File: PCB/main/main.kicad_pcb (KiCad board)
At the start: 2 copper layers, 4 parts, among them J1 Conn_01x33_Female, J2 Conn_01x33_Female, J3 Conn_01x33_Female, J4 Conn_01x33_Female

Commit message: Design PCB
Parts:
- added BT1: 18650, Footprint_EEE3088F:18650_Holder, F.Cu at (128.0, 139.8)
- added C1: 0.1uF, Capacitor_SMD:C_0402_1005Metric, F.Cu at (171.6, 112.8)
- added C10: 100nF, Capacitor_SMD:C_0402_1005Metric, F.Cu at (86.9, 85.4)
- added C11: 4.7nF, Capacitor_SMD:C_0402_1005Metric, F.Cu at (91.5, 85.4)
- added C2: 22uF, Capacitor_SMD:C_0603_1608Metric, F.Cu at (167.2, 98.6)
- added C3: 330pF, Capacitor_SMD:C_0402_1005Metric, F.Cu at (159.0, 98.0)
- added C4: 0.1uF, Capacitor_SMD:C_0402_1005Metric, F.Cu at (133.0, 156.8)
- added C5: 100uF, Capacitor_SMD:C_1206_3216Metric, F.Cu at (133.0, 161.4)
- added C6: 33pF, Capacitor_SMD:C_0402_1005Metric, F.Cu at (151.2, 88.6)
- added C7: 10nF, Capacitor_SMD:C_0402_1005Metric, F.Cu at (158.2, 93.6)
- added C8: 33pF, Capacitor_SMD:C_0402_1005Metric, F.Cu at (151.4, 80.2)
- added C9: 0.1uF, Capacitor_SMD:C_0402_1005Metric, F.Cu at (151.8, 103.8)
- added D1: BAT54S, Diode_SMD:D_SOT-23_ANK, F.Cu at (177.8, 141.4)
- added D2: DIODE, Footprint_EEE3088F:DO-214AC_L4.3-W2.7-LS5.3-RD, F.Cu at (171.2, 99.6)
- added D3: ZMM5V1-M, Footprint_EEE3088F:LL-34_L3.5-W1.5-RD, F.Cu at (180.7, 112.2)
- added D4: LED, LED_SMD:LED_0603_1608Metric, F.Cu at (171.0, 93.2)
- added D5: ZMM4V7-M, Footprint_EEE3088F:LL-34_L3.5-W1.5-RD, F.Cu at (170.5, 153.2)
- added D6: DIODE, Footprint_EEE3088F:DO-214AC_L4.3-W2.7-LS5.3-RD, F.Cu at (160.0, 156.6)
- added D7: BZT52C3V0, Diode_SMD:D_SOD-123, F.Cu at (106.0, 97.8)
- added D8: LED, LED_SMD:LED_0603_1608Metric, F.Cu at (93.2, 93.2)
- added D9: LED, LED_SMD:LED_0603_1608Metric, F.Cu at (93.3, 116.3)
- added J1: Conn_01x03_Female, Connector_PinHeader_1.00mm:PinHeader_1x03_P1.00mm_Vertical, F.Cu at (180.0, 132.6)
- added JP1: SolderJumper_2_Bridged, Jumper:SolderJumper-2_P1.3mm_Bridged2Bar_Pad1.0x1.5mm, F.Cu at (175.8, 112.2)
- added JP10: SolderJumper_2_Bridged, Jumper:SolderJumper-2_P1.3mm_Bridged2Bar_Pad1.0x1.5mm, F.Cu at (148.0, 109.4)
- added JP2: SolderJumper_2_Bridged, Jumper:SolderJumper-2_P1.3mm_Bridged2Bar_Pad1.0x1.5mm, F.Cu at (175.3, 103.4)
- added JP3: SolderJumper_2_Bridged, Jumper:SolderJumper-2_P1.3mm_Bridged2Bar_Pad1.0x1.5mm, F.Cu at (173.6, 141.6)
- added JP4: SolderJumper_2_Bridged, Jumper:SolderJumper-2_P1.3mm_Bridged2Bar_Pad1.0x1.5mm, F.Cu at (133.2, 152.8)
- added JP5: SolderJumper_2_Bridged, Jumper:SolderJumper-2_P1.3mm_Bridged2Bar_Pad1.0x1.5mm, F.Cu at (88.9, 104.9)
- added JP6: SolderJumper_2_Bridged, Jumper:SolderJumper-2_P1.3mm_Bridged2Bar_Pad1.0x1.5mm, F.Cu at (88.8, 96.6)
- added JP7: SolderJumper_2_Bridged, Jumper:SolderJumper-2_P1.3mm_Bridged2Bar_Pad1.0x1.5mm, F.Cu at (166.8, 81.0)
- added JP8: SolderJumper_2_Bridged, Jumper:SolderJumper-2_P1.3mm_Bridged2Bar_Pad1.0x1.5mm, F.Cu at (167.0, 85.4)
- added JP9: SolderJumper_2_Bridged, Jumper:SolderJumper-2_P1.3mm_Bridged2Bar_Pad1.0x1.5mm, F.Cu at (143.4, 109.5)
- added K1: ADW11, Relay_THT:Relay_SPST_Omron-G5Q-1A, F.Cu at (155.6, 152.8)
- added Q1: AO3401A, Package_TO_SOT_SMD:SOT-23, F.Cu at (180.6, 104.0)
- added Q2: 2N3904, Package_TO_SOT_SMD:SOT-23, F.Cu at (166.2, 157.6)
- added Q3: FDS6690A, Package_SO:SOIC-8_3.9x4.9mm_P1.27mm, F.Cu at (102.6, 109.1)
- added R1: 100, Resistor_SMD:R_0603_1608Metric, F.Cu at (179.8, 108.2)
- added R10: 1k, Resistor_SMD:R_0402_1005Metric, F.Cu at (182.1, 153.2)
- added R11: 100k, Resistor_SMD:R_0402_1005Metric, F.Cu at (175.0, 153.3)
- added R12: 330, Resistor_SMD:R_0402_1005Metric, F.Cu at (97.1, 97.8)
- added R13: 330, Resistor_SMD:R_0402_1005Metric, F.Cu at (100.5, 97.8)
- added R14: 10k, Resistor_SMD:R_0402_1005Metric, F.Cu at (93.2, 89.2)
- added R15: 330, Resistor_SMD:R_0402_1005Metric, F.Cu at (93.6, 105.6)
- added R16: 220, Resistor_SMD:R_0402_1005Metric, F.Cu at (93.6, 109.1)
- added R17: 10k, Resistor_SMD:R_0402_1005Metric, F.Cu at (93.6, 112.9)
- added R2: 2M, Resistor_SMD:R_0805_2012Metric, F.Cu at (163.0, 97.9)
- added R3: 806K, Resistor_SMD:R_0402_1005Metric, F.Cu at (159.0, 101.4)
- added R4: 2.7k, Resistor_SMD:R_0402_1005Metric, F.Cu at (167.3, 93.2)
- added R5: 4.7k, Resistor_SMD:R_0402_1005Metric, F.Cu at (163.6, 93.2)
- added R6: 82, Resistor_SMD:R_0603_1608Metric, F.Cu at (171.0, 89.0)
- added R7: 10k, Resistor_SMD:R_0402_1005Metric, F.Cu at (154.1, 109.6)
- added R8: 10k, Resistor_SMD:R_0402_1005Metric, F.Cu at (154.1, 113.0)
- added R9: 150, Resistor_SMD:R_0402_1005Metric, F.Cu at (178.6, 153.2)
- added RV1: 50K, Footprint_EEE3088F:VG039NCHXTB503, F.Cu at (159.0, 107.4)
- added TP1: TestPoint, TestPoint:TestPoint_Pad_D1.0mm, B.Cu at (169.4, 148.4)
- added TP2: TestPoint, TestPoint:TestPoint_Pad_D1.0mm, B.Cu at (154.0, 98.5)
- added TP3: TestPoint, TestPoint:TestPoint_Pad_D1.0mm, B.Cu at (165.5, 90.2)
- added TP4: TestPoint, TestPoint:TestPoint_Pad_D1.0mm, B.Cu at (147.5, 147.1)
- added TP5: TestPoint, TestPoint:TestPoint_Pad_D1.0mm, B.Cu at (99.2, 102.4)
- added TP6: TestPoint, TestPoint:TestPoint_Pad_D1.0mm, B.Cu at (157.4, 112.3)
- added U1: LP2951-33DR, Package_SO:SOIC-8_3.9x4.9mm_P1.27mm, F.Cu at (169.2, 107.6)
- added U2: AMS1117, Package_TO_SOT_SMD:SOT-223-3_TabPin2, F.Cu at (125.0, 155.2)
- added U3: CH340G, Package_SO:SOIC-16_3.9x9.9mm_P1.27mm, F.Cu at (158.2, 85.0)
- added U4: USB_Micro_B, Footprint_EEE3088F:C404969_Micro_USB, F.Cu at (184.2, 96.5)
- added U5: AT24C256C-SSHL-T, Footprint_EEE3088F:SOIC-8_L4.9-W3.9-P1.27-LS6.0-BL, F.Cu at (147.2, 100.6)
- added U6: LM358DR2G, Package_SO:SOIC-8_3.9x4.9mm_P1.27mm, F.Cu at (178.6, 158.8)
- added U7: VL6180XV0NR_1, Footprint_EEE3088F:LGA-12_L4.8-W2.8-P0.75-BL, F.Cu at (88.8, 90.6)
- added U8: MCP9700T-ETT, Package_TO_SOT_SMD:SOT-23, F.Cu at (88.7, 110.2)
- added X1: 12MHz Crystal, Footprint_EEE3088F:OSC-SMD_4P-L3.2-W2.5-BL, F.Cu at (151.4, 84.2)
- J3: renamed from J2; footprint Connector_PinSocket_2.54mm:PinSocket_1x33_P2.54mm_Vertical -> Connector_PinHeader_2.54mm:PinHeader_1x33_P2.54mm_Vertical
- J4: renamed from J3; footprint Connector_PinSocket_2.54mm:PinSocket_1x33_P2.54mm_Vertical -> Connector_PinHeader_2.54mm:PinHeader_1x33_P2.54mm_Vertical
- renumbered J1 to J2, J4 to J5
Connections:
- net +3V0 renamed /+3V0
- net +5V renamed /+5V
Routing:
- net VDD: track 0.00 -> 212.7 mm, vias 0 -> 3
- net /Power/Battery +: track 0.00 -> 131.3 mm, vias 0 -> 2
- net /PB8: track 0.00 -> 110.9 mm, vias 0 -> 6
- net /PB7: track 0.00 -> 98.6 mm, vias 0 -> 2
- net /PB4: track 0.00 -> 90.4 mm
- net /microcontroller_interfacing/+5V: track 0.00 -> 86.5 mm
- net GND: track 0.00 -> 77.1 mm, vias 0 -> 12
- net /PA4: track 0.00 -> 62.4 mm, vias 0 -> 1
- net /PA9: track 0.00 -> 61.3 mm, vias 0 -> 2
- net /PA10: track 0.00 -> 58.2 mm, vias 0 -> 2
- net /Power/+5V (REVERSE PROTECTED): track 0.00 -> 49.9 mm, vias 0 -> 2
- net /PB1: track 0.00 -> 43.9 mm
- net /PB0: track 0.00 -> 43.6 mm, vias 0 -> 2
- net /Sensing/Proximity_Sensor/VCC: track 0.00 -> 33.6 mm
- net Net-(C8-Pad1): track 0.00 -> 27.0 mm, vias 0 -> 2
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- added copper zone on B.Cu, net (none)
- added copper zone on F.Cu, net GND
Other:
- board outline added: 100 x 100 mm
- board text added: "Heather, Kelvin, Noah Group 5"

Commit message: Fix DRC errors
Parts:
- J1: footprint Connector_PinHeader_1.00mm:PinHeader_1x03_P1.00mm_Vertical -> Connector_PinHeader_1.27mm:PinHeader_1x03_P1.27mm_Vertical

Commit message: pcb revive
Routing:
- net /Power/Battery +: track 131.3 -> 150.6 mm
- net Net-(C8-Pad1): track 27.0 -> 29.1 mm
- net /Sensing/Proximity_Sensor/VCC: track 33.7 -> 31.7 mm
- net Net-(C3-Pad2): track 20.6 -> 22.6 mm
- net VDD: track 212.8 -> 214.5 mm
- net Net-(D5-Pad1): track 15.5 -> 13.9 mm
- net /microcontroller_interfacing/D-: track 19.8 -> 21.1 mm
- net /PB7: track 98.6 -> 99.3 mm
- net /PB4: track 90.4 -> 90.9 mm

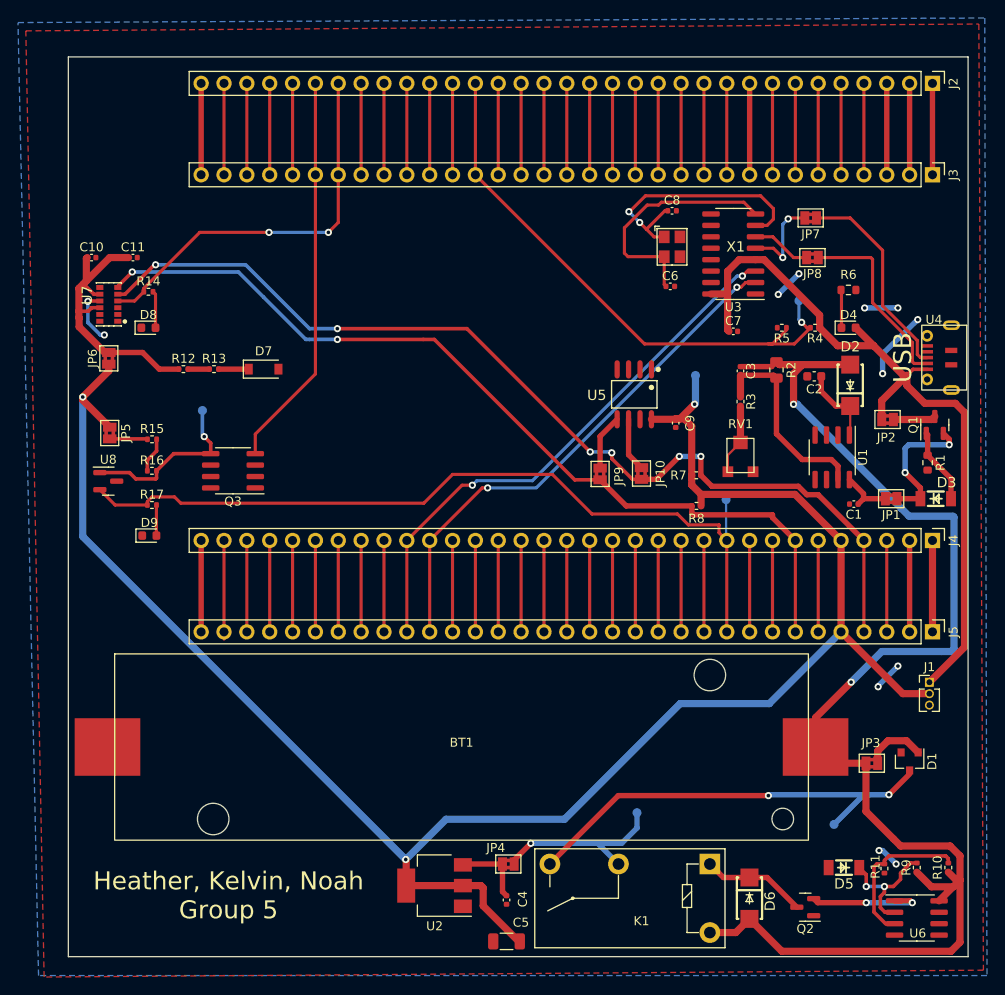
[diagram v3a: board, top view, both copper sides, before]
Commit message: Revert "pcb n"
This reverts commit 8727529f109f5bdd44d95993405a88df4b4ab9b1
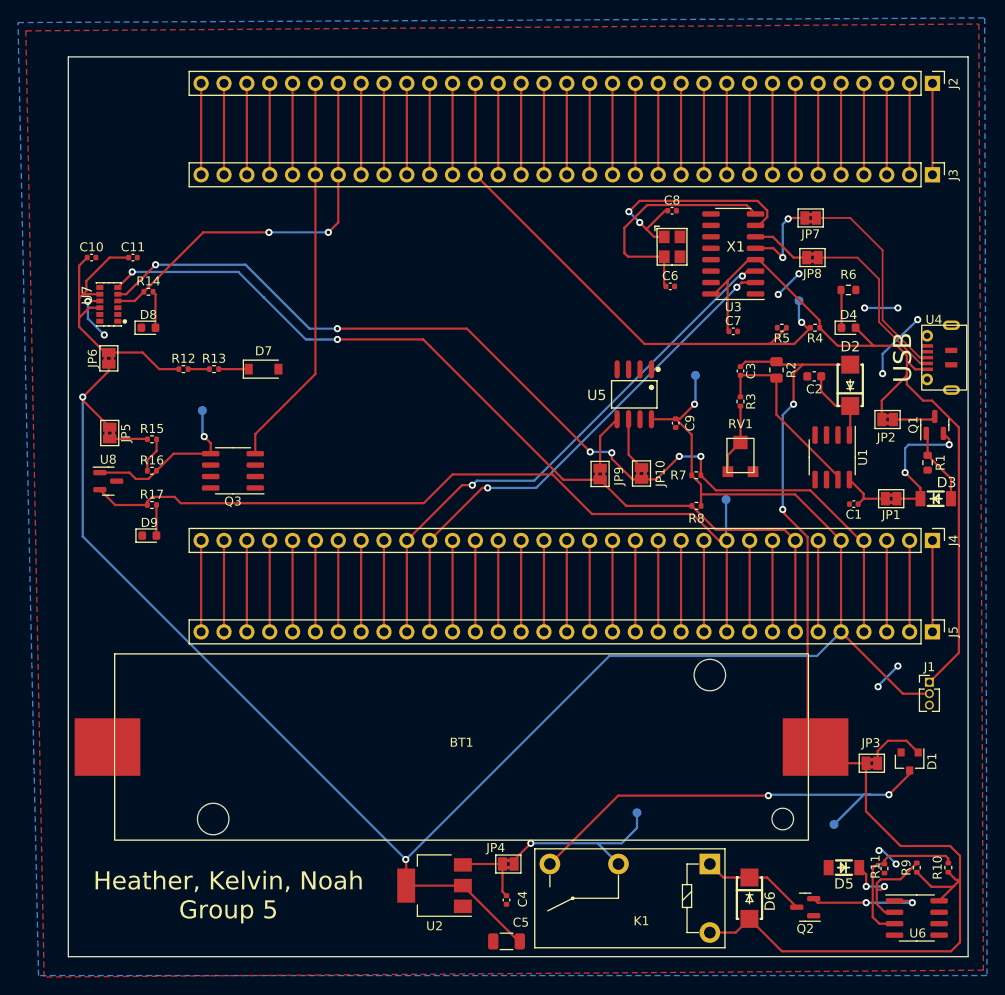
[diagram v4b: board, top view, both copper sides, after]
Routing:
- net /Power/Battery +: track 150.6 -> 131.3 mm
- net Net-(C8-Pad1): track 29.1 -> 27.0 mm
- net /Sensing/Proximity_Sensor/VCC: track 31.7 -> 33.7 mm
- net Net-(C3-Pad2): track 22.6 -> 20.6 mm
- net VDD: track 214.5 -> 212.8 mm
- net Net-(D5-Pad1): track 13.9 -> 15.5 mm
- net /microcontroller_interfacing/D-: track 21.1 -> 19.8 mm
- net /PB7: track 99.3 -> 98.6 mm
- net /PB4: track 90.9 -> 90.4 mm

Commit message: Add header
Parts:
- J1: value Conn_01x03_Female -> Conn_01x10_Male; footprint Connector_PinHeader_1.27mm:PinHeader_1x03_P1.27mm_Vertical -> Connector_PinHeader_2.54mm:PinHeader_1x10_P2.54mm_Vertical
- K1: value ADW11 -> G5NB
- Q2: value 2N3904 -> MMBT3904
- moved J1 90.1 mm to (92.2, 153.1), turned to 90 degrees
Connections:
- J1 pad 2: VDD -> /PB4
- J1 pad 3: GND -> /PB7
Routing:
- net /microcontroller_interfacing/+5V: track 86.5 -> 186.1 mm, vias 0 -> 4
- net /PA4: track 62.4 -> 142.6 mm, vias 1 -> 3
- net /PB8: track 110.9 -> 183.9 mm, vias 6 -> 7
- net /PB7: track 98.6 -> 164.9 mm, vias 2 -> 3
- net /PB4: track 90.4 -> 133.3 mm, vias 0 -> 2
- net /PA9: track 61.3 -> 92.4 mm
- net /PA10: track 58.2 -> 89.3 mm
- net VDD: track 212.8 -> 200.1 mm
- net GND: track 77.0 -> 73.8 mm, vias 12 -> 10

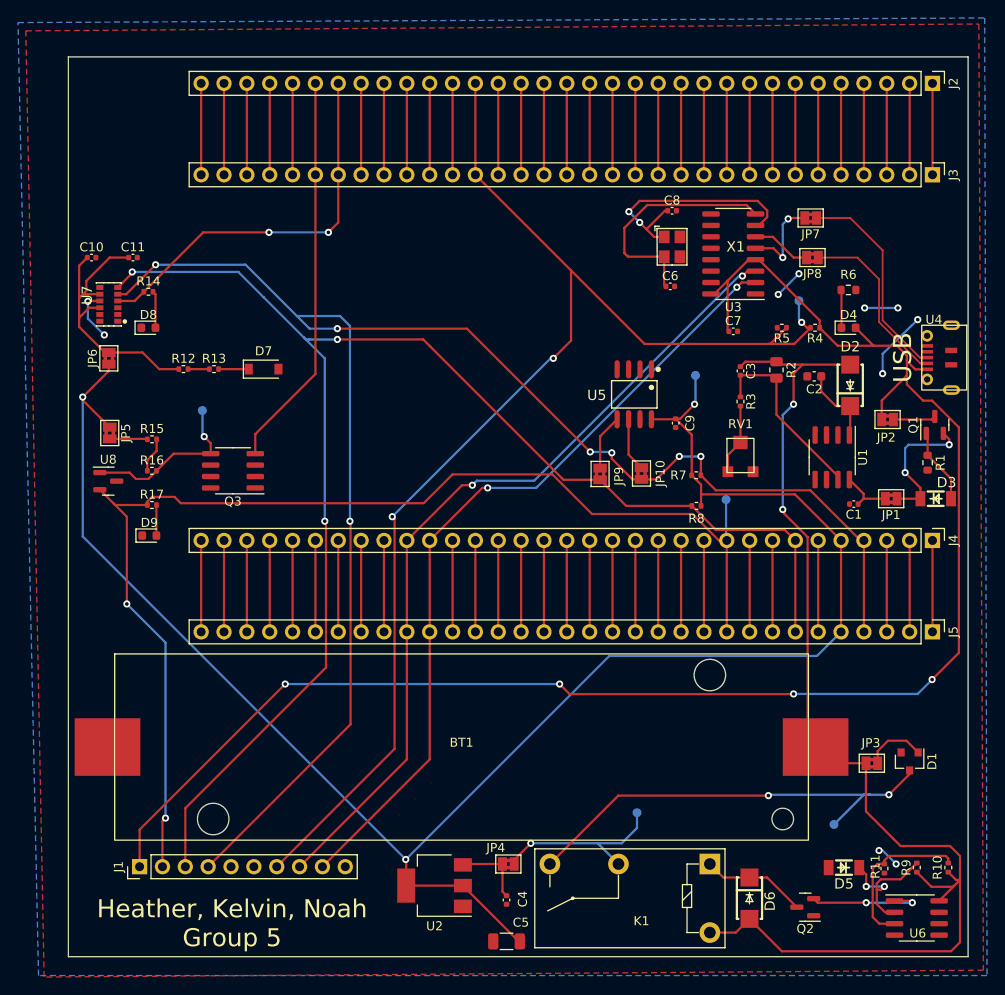
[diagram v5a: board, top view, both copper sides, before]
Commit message: Add labels
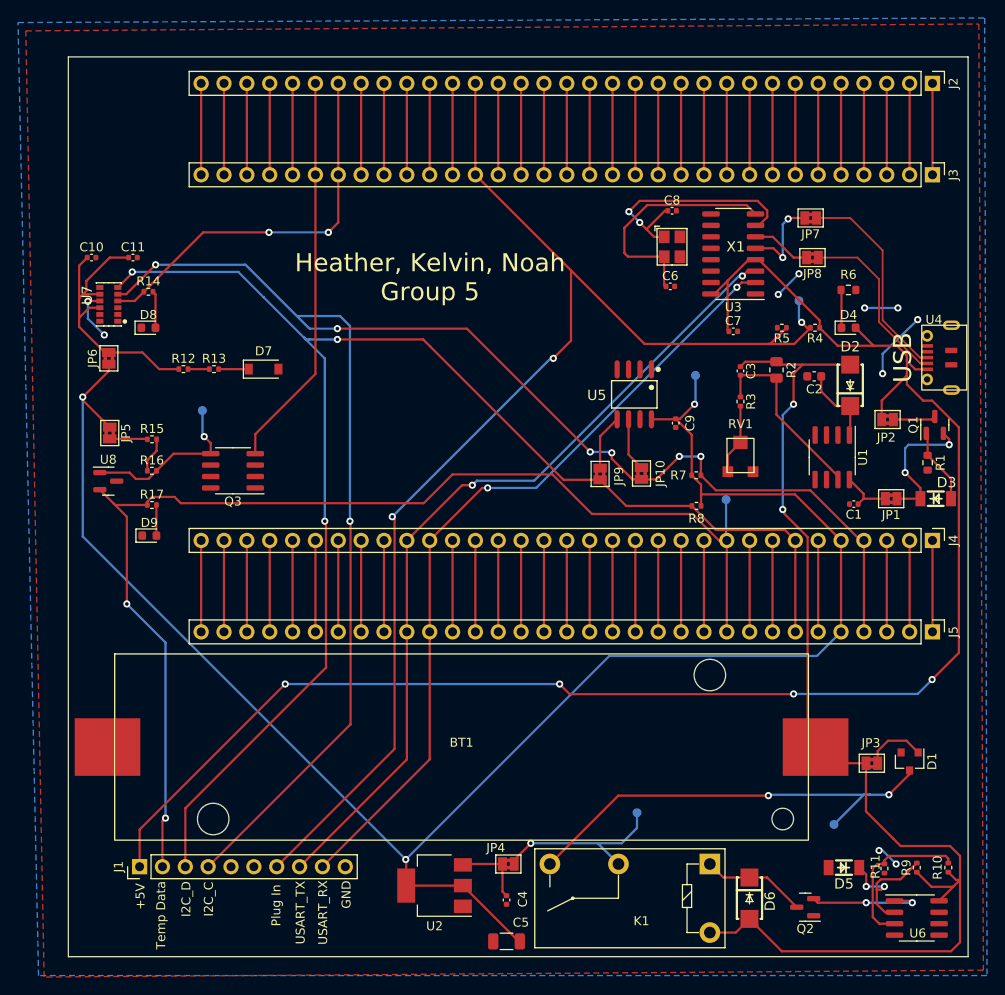
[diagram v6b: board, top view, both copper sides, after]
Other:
- board text added: "+5V"
- board text added: "GND"
- board text added: "I2C_C"
- board text added: "I2C_D"
- board text added: "Plug In"
- board text added: "Temp Data"
- board text added: "USART_RX"
- board text added: "USART_TX"
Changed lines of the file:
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@@
   (gr_line (start 184.15 123.19) (end 95.25 123.19) (layer "F.Fab") (width 0.1))
   (gr_rect (start 173.99 91.44) (end 184.15 101.6) (layer "F.Fab") (width 0.1) (fill none))
+  (gr_text "GND" (at 115.2 156.2 90) (layer "F.SilkS")
+    (effects (font (size 1 1) (thickness 0.15)))
+  )
+  (gr_text "USART_RX" (at 112.6 158.2 90) (layer "F.SilkS")
+    (effects (font (size 1 1) (thickness 0.15)))
+  )
+  (gr_text "Plug In" (at 107.4 157.4 90) (layer "F.SilkS")
+    (effects (font (size 1 1) (thickness 0.15)))
+  )
+  (gr_text "USART_TX" (at 110.1 158.2 90) (layer "F.SilkS")
+    (effects (font (size 1 1) (thickness 0.15)))
+  )
+  (gr_text "I2C_C" (at 99.9 156.7 90) (layer "F.SilkS")
+    (effects (font (size 1 1) (thickness 0.15)))
+  )
+  (gr_text "+5V" (at 92.3 156.4 90) (layer "F.SilkS")
+    (effects (font (size 1 1) (thickness 0.15)))
+  )
+  (gr_text "Temp Data" (at 94.6 158.5 90) (layer "F.SilkS")
+    (effects (font (size 1 1) (thickness 0.15)))
+  )
   (gr_text "USB" (at 177.038 96.52 90) (layer "F.SilkS")
     (effects (font (size 2 2) (thickness 0.3)))
   )
-  (gr_text "Heather, Kelvin, Noah\nGroup 5" (at 102.5 159.4) (layer "F.SilkS")
+  (gr_text "Heather, Kelvin, Noah\nGroup 5" (at 124.5 87.6) (layer "F.SilkS")
     (effects (font (size 2 2) (thickness 0.25)))
   )
+  (gr_text "I2C_D" (at 97.4 156.7 90) (layer "F.SilkS")
+    (effects (font (size 1 1) (thickness 0.15)))
+  )
   (gr_text "USB" (at 177.038 96.52 90) (layer "F.Fab")
